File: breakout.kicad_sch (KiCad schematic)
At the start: 14 parts, among them J1 Conn_01x04, J2 Conn_01x02, J3 Conn_01x02, Q1 MMBT3904, Q2 MMBT3904

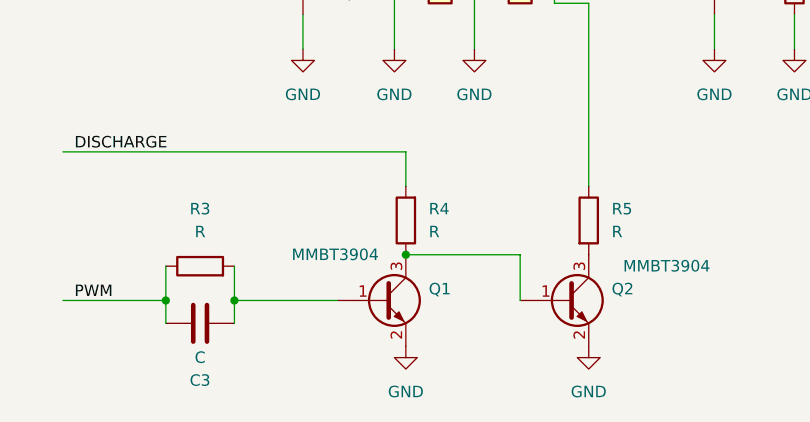
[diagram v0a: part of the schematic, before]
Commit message: create panel
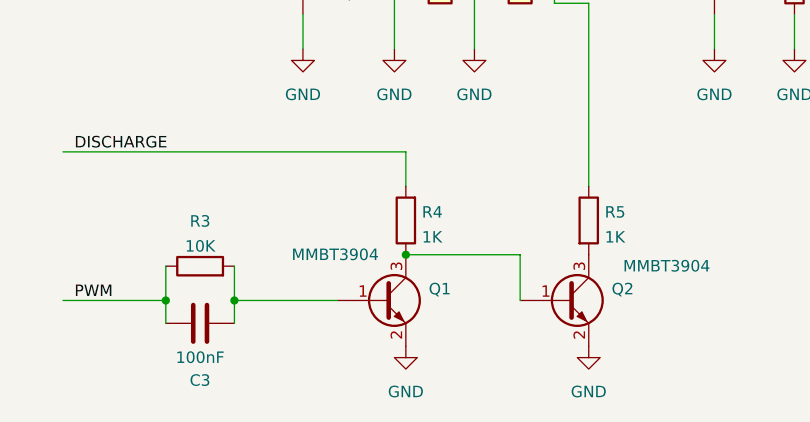
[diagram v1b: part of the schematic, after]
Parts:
- C1: LCSC Part (none) -> C1669
- C2: LCSC Part (none) -> C1588
- C3: value C -> 100nF; LCSC Part (none) -> C14858
- D1: LCSC Part (none) -> C8598
- Q1, Q2: LCSC Part (none) -> C20526
- R1: LCSC Part (none) -> C25804
- R2: LCSC Part (none) -> C22935
- R3: value R -> 10K; LCSC Part (none) -> C25804
- R4, R5: value R -> 1K; LCSC Part (none) -> C21190
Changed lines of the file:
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@@
   (symbol (lib_id "Device:R") (at 152.4 97.79 180) (unit 1)
     (in_bom yes) (on_board yes) (fields_autoplaced)
-    (property "Reference" "R4" (id 0) (at 154.94 96.5199 0)
+    (property "Reference" "R4" (id 0) (at 154.178 96.8815 0)
       (effects (font (size 1.27 1.27)) (justify right))
     )
-    (property "Value" "R" (id 1) (at 154.94 99.0599 0)
+    (property "Value" "1K" (id 1) (at 154.178 99.6566 0)
       (effects (font (size 1.27 1.27)) (justify right))
     )
@@
     )
     (property "Datasheet" "~" (id 3) (at 152.4 97.79 0)
+      (effects (font (size 1.27 1.27)) hide)
+    )
+    (property "LCSC Part" "C21190" (id 4) (at 152.4 97.79 0)
       (effects (font (size 1.27 1.27)) hide)
     )
@@
       (effects (font (size 1.27 1.27)) hide)
     )
+    (property "LCSC Part" "C1588" (id 4) (at 186.69 71.12 0)
+      (effects (font (size 1.27 1.27)) hide)
+    )
     (pin "1")
     (pin "2")
@@
       (effects (font (size 1.27 1.27)) hide)
     )
+    (property "LCSC Part" "C22935" (id 4) (at 195.58 71.12 0)
+      (effects (font (size 1.27 1.27)) hide)
+    )
     (pin "1")
     (pin "2")
@@
   (symbol (lib_id "Device:R") (at 129.54 102.87 90) (unit 1)
     (in_bom yes) (on_board yes) (fields_autoplaced)
-    (property "Reference" "R3" (id 0) (at 129.54 96.52 90))
-    (property "Value" "R" (id 1) (at 129.54 99.06 90))
+    (property "Reference" "R3" (id 0) (at 129.54 97.8875 90))
+    (property "Value" "10K" (id 1) (at 129.54 100.6626 90))
     (property "Footprint" "Resistor_SMD:R_0603_1608Metric" (id 2) (at 129.54 104.648 90)
       (effects (font (size 1.27 1.27)) hide)
     )
     (property "Datasheet" "~" (id 3) (at 129.54 102.87 0)
+      (effects (font (size 1.27 1.27)) hide)
+    )
+    (property "LCSC Part" "C25804" (id 4) (at 129.54 102.87 90)
       (effects (font (size 1.27 1.27)) hide)
     )
@@
       (effects (font (size 1.27 1.27)) hide)
     )
+    (property "LCSC Part" "C25804" (id 4) (at 129.54 64.77 90)
+      (effects (font (size 1.27 1.27)) hide)
+    )
     (pin "1")
     (pin "2")
@@
       (effects (font (size 1.27 1.27)) hide)
     )
+    (property "LCSC Part" "C1669" (id 4) (at 140.97 71.12 0)
+      (effects (font (size 1.27 1.27)) hide)
+    )
     (pin "1")
     (pin "2")
@@
     (in_bom yes) (on_board yes)
     (property "Reference" "C3" (id 0) (at 129.54 115.57 90))
-    (property "Value" "C" (id 1) (at 129.54 113.03 90))
+    (property "Value" "100nF" (id 1) (at 129.54 113.03 90))
     (property "Footprint" "Capacitor_SMD:C_0603_1608Metric" (id 2) (at 125.73 110.1852 0)
       (effects (font (size 1.27 1.27)) hide)
     )
     (property "Datasheet" "~" (id 3) (at 129.54 109.22 0)
+      (effects (font (size 1.27 1.27)) hide)
+    )
+    (property "LCSC Part" "C14858" (id 4) (at 129.54 109.22 90)
       (effects (font (size 1.27 1.27)) hide)
     )
@@
       (effects (font (size 1.27 1.27)) hide)
     )
+    (property "LCSC Part" "C8598" (id 4) (at 177.8 64.77 0)
+      (effects (font (size 1.27 1.27)) hide)
+    )
     (pin "1")
     (pin "2")
@@
       (effects (font (size 1.27 1.27)) (justify left) hide)
     )
+    (property "LCSC Part" "C20526" (id 4) (at 170.18 106.68 0)
+      (effects (font (size 1.27 1.27)) hide)
+    )
     (pin "1")
     (pin "2")
@@
   (symbol (lib_id "Device:R") (at 172.72 97.79 0) (unit 1)
     (in_bom yes) (on_board yes) (fields_autoplaced)
-    (property "Reference" "R5" (id 0) (at 175.26 96.5199 0)
-      (effects (font (size 1.27 1.27)) (justify left))
-    )
-    (property "Value" "R" (id 1) (at 175.26 99.0599 0)
+    (property "Reference" "R5" (id 0) (at 174.498 96.8815 0)
+      (effects (font (size 1.27 1.27)) (justify left))
+    )
+    (property "Value" "1K" (id 1) (at 174.498 99.6566 0)
       (effects (font (size 1.27 1.27)) (justify left))
     )
@@
     )
     (property "Datasheet" "~" (id 3) (at 172.72 97.79 0)
+      (effects (font (size 1.27 1.27)) hide)
+    )
+    (property "LCSC Part" "C21190" (id 4) (at 172.72 97.79 0)
       (effects (font (size 1.27 1.27)) hide)
     )
@@
     (property "Datasheet" "https://www.onsemi.com/pub/Collateral/2N3903-D.PDF" (id 3) (at 149.86 106.68 0)
       (effects (font (size 1.27 1.27)) (justify left) hide)
+    )
+    (property "LCSC Part" "C20526" (id 4) (at 149.86 106.68 0)
+      (effects (font (size 1.27 1.27)) hide)
     )
     (pin "1")
@@
     )
     (path "/6811506d-a5ef-4cb1-8084-d2474c50be8b"
-      (reference "C3") (unit 1) (value "C") (footprint "Capacitor_SMD:C_0603_1608Metric")
+      (reference "C3") (unit 1) (value "100nF") (footprint "Capacitor_SMD:C_0603_1608Metric")
     )
     (path "/6b390b1c-859e-4d1f-813d-3d748dde0e47"
@@
     )
     (path "/21a079b8-d67a-400b-861b-4f1a758b8d19"
-      (reference "R3") (unit 1) (value "R") (footprint "Resistor_SMD:R_0603_1608Metric")
+      (reference "R3") (unit 1) (value "10K") (footprint "Resistor_SMD:R_0603_1608Metric")
     )
     (path "/0326f230-c310-472b-8a34-060ea1eb39ed"
-      (reference "R4") (unit 1) (value "R") (footprint "Resistor_SMD:R_0603_1608Metric")
+      (reference "R4") (unit 1) (value "1K") (footprint "Resistor_SMD:R_0603_1608Metric")
     )
     (path "/a2a2f7b4-e45b-4bad-bd28-df22f89e875a"
-      (reference "R5") (unit 1) (value "R") (footprint "Resistor_SMD:R_0603_1608Metric")
-    )
-  )
+      (reference "R5") (unit 1) (value "1K") (footprint "Resistor_SMD:R_0603_1608Metric")
+    )
+  )
